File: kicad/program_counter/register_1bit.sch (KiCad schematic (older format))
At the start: 5 parts, among them U1 SN74ALVC00, U2 SN74ALVC00, U3 SN74ALVC00, U4 SN74ALVC00, U5 SN74ALVC00

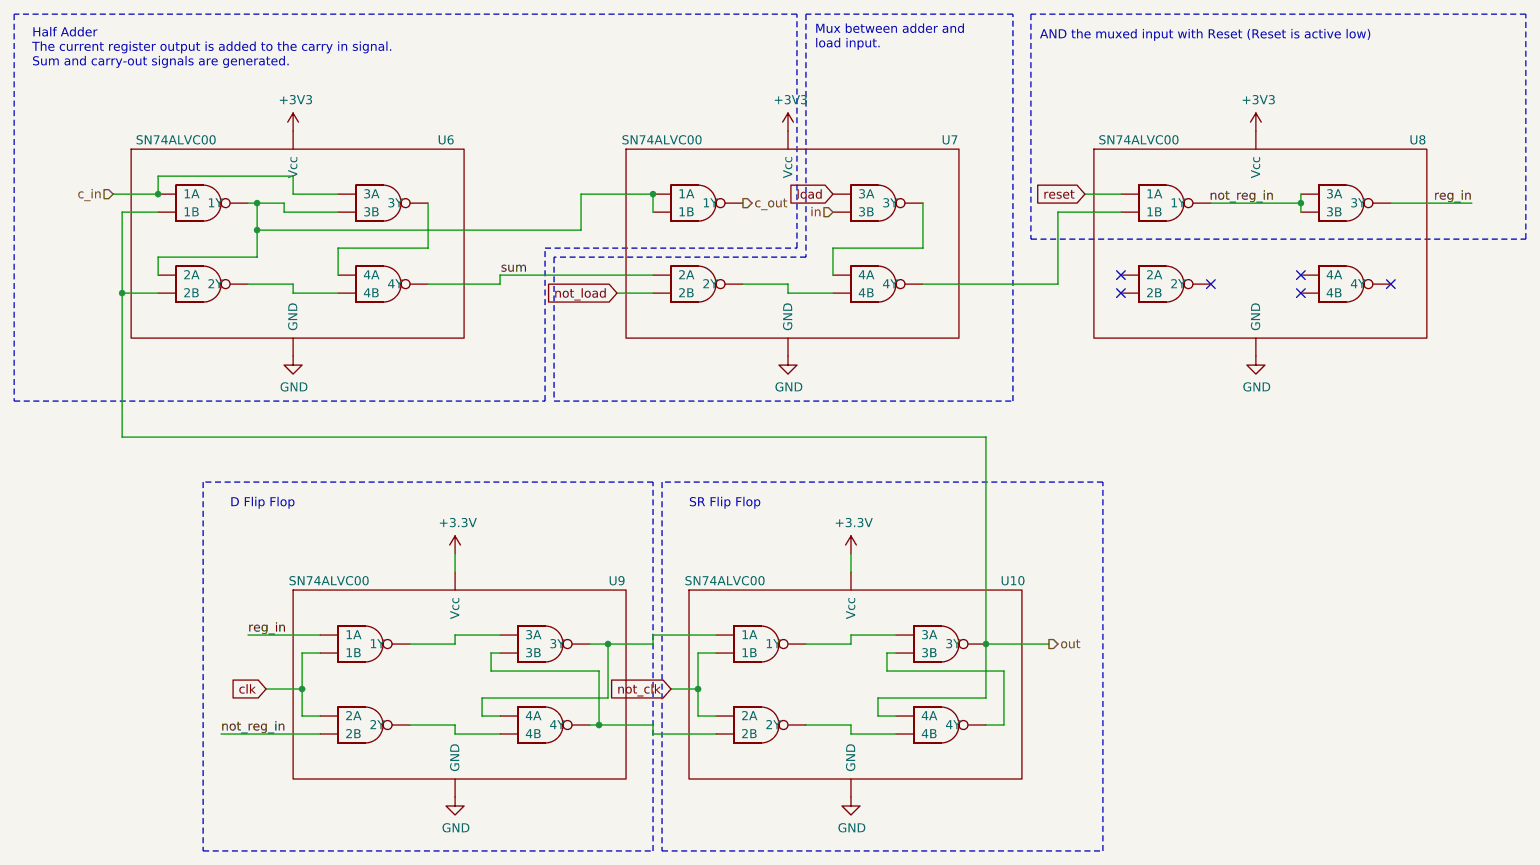
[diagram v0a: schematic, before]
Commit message: ALU schematic, layout, routing complete. Associated motherboardmod. Also added Load LED to register and program counter boards.
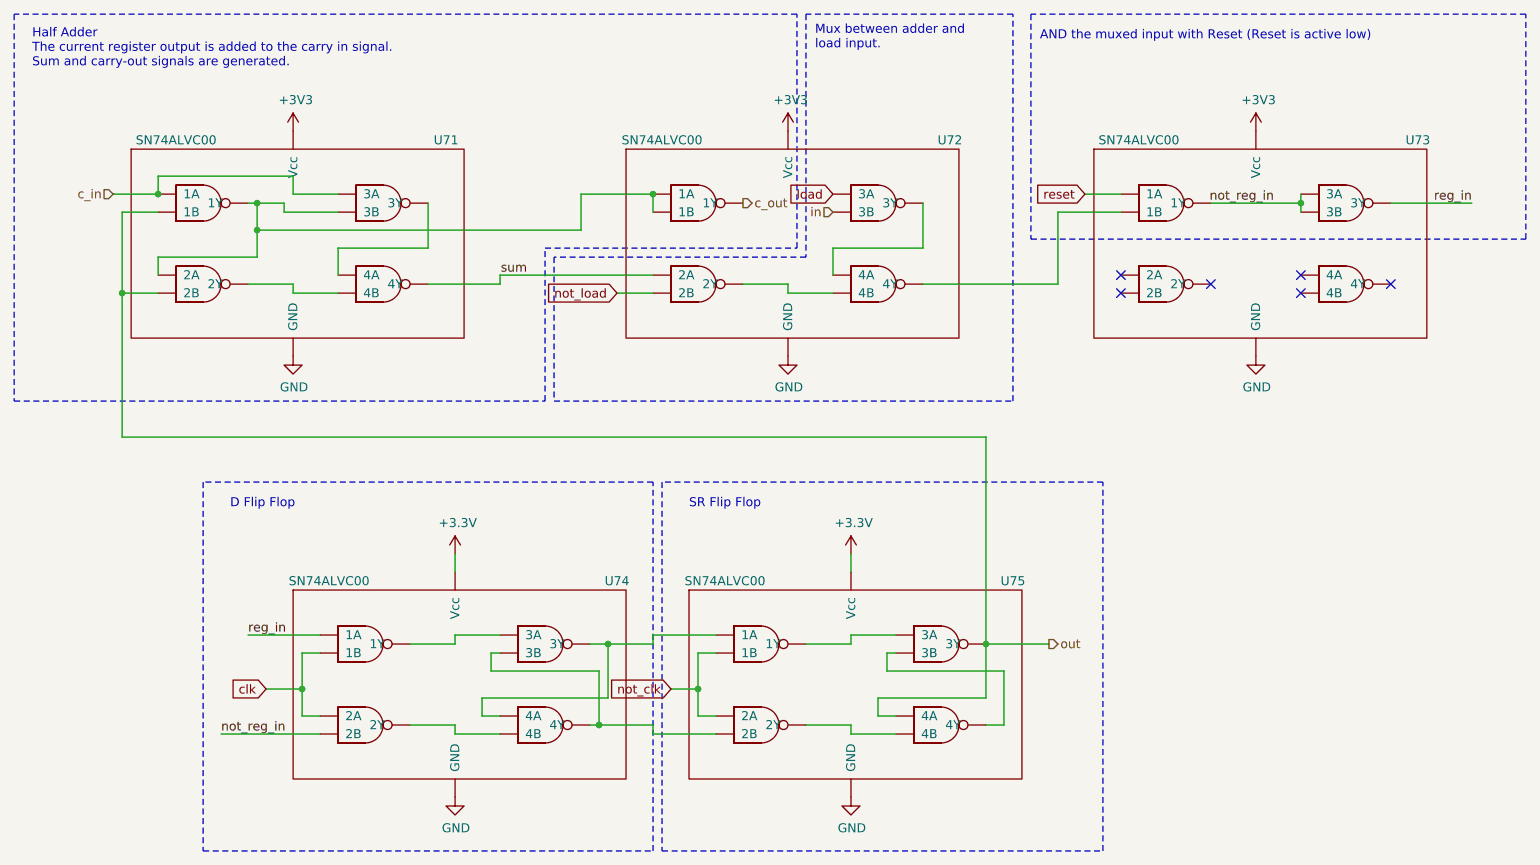
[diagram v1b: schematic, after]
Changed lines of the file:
@@
 $Descr A4 11693 8268
 encoding utf-8
-Sheet 2 16
+Sheet 11 16
 Title "1-bit Register"
 Date "2020-03-15"
@@
 AR Path="/5EC1DD9B/5E702849" Ref="U15"  Part="1"
 AR Path="/5EC1DDBF/5E702849" Ref="U10"  Part="1"
-F 0 "U10" H 7450 3800 50  0000 C CNN
+F 0 "U75" H 7450 3800 50  0000 C CNN
 F 1 "SN74ALVC00" H 5850 3800 50  0000 C CNN
 F 2 "Package_SO:TSSOP-14_4.4x5mm_P0.65mm" H 6550 2650 50  0001 C CNN
@@
 AR Path="/5EC1DD9B/5E6F4B7A" Ref="U14"  Part="1"
 AR Path="/5EC1DDBF/5E6F4B7A" Ref="U9"  Part="1"
-F 0 "U9" H 5250 3800 50  0000 C CNN
+F 0 "U74" H 5250 3800 50  0000 C CNN
 F 1 "SN74ALVC00" H 3650 3800 50  0000 C CNN
 F 2 "Package_SO:TSSOP-14_4.4x5mm_P0.65mm" H 4350 2650 50  0001 C CNN
@@
 AR Path="/5EC1DD9B/5EA8676E" Ref="U13"  Part="1"
 AR Path="/5EC1DDBF/5EA8676E" Ref="U8"  Part="1"
-F 0 "U8" H 9700 1350 50  0000 C CNN
+F 0 "U73" H 9700 1350 50  0000 C CNN
 F 1 "SN74ALVC00" H 8150 1350 50  0000 C CNN
 F 2 "Package_SO:TSSOP-14_4.4x5mm_P0.65mm" H 8800 200 50  0001 C CNN
@@
 AR Path="/5EC1DD9B/5EA8671D" Ref="U12"  Part="1"
 AR Path="/5EC1DDBF/5EA8671D" Ref="U7"  Part="1"
-F 0 "U7" H 7100 1350 50  0000 C CNN
+F 0 "U72" H 7100 1350 50  0000 C CNN
 F 1 "SN74ALVC00" H 5500 1350 50  0000 C CNN
 F 2 "Package_SO:TSSOP-14_4.4x5mm_P0.65mm" H 6200 200 50  0001 C CNN
@@
 AR Path="/5EC1DD9B/5EA86726" Ref="U11"  Part="1"
 AR Path="/5EC1DDBF/5EA86726" Ref="U6"  Part="1"
-F 0 "U6" H 4300 1350 50  0000 C CNN
+F 0 "U71" H 4300 1350 50  0000 C CNN
 F 1 "SN74ALVC00" H 2800 1350 50  0000 C CNN
 F 2 "Package_SO:TSSOP-14_4.4x5mm_P0.65mm" H 3450 200 50  0001 C CNN

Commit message: Readme updates (#6)
* Readme intro section

* Board revisions for manufacturing, add digikey PNs to all, added logo.
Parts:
- U1, U2, U3, U4, U5: Digikey PN (none) -> 296-5104-1-ND
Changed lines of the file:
@@
 $Descr A4 11693 8268
 encoding utf-8
-Sheet 11 16
+Sheet 13 16
 Title "1-bit Register"
 Date "2020-03-15"
@@
 F 2 "Package_SO:TSSOP-14_4.4x5mm_P0.65mm" H 6550 2650 50  0001 C CNN
 F 3 "" H 6800 4150 50  0001 C CNN
+F 4 "296-5104-1-ND" H 0   0   50  0001 C CNN "Digikey PN"
 	1    6800 4150
 	1    0    0    -1
@@
 F 2 "Package_SO:TSSOP-14_4.4x5mm_P0.65mm" H 4350 2650 50  0001 C CNN
 F 3 "" H 4600 4150 50  0001 C CNN
+F 4 "296-5104-1-ND" H 0   0   50  0001 C CNN "Digikey PN"
 	1    4600 4150
 	1    0    0    -1
@@
 F 2 "Package_SO:TSSOP-14_4.4x5mm_P0.65mm" H 8800 200 50  0001 C CNN
 F 3 "" H 9050 1700 50  0001 C CNN
+F 4 "296-5104-1-ND" H 0   0   50  0001 C CNN "Digikey PN"
 	1    9050 1700
 	1    0    0    -1
@@
 F 2 "Package_SO:TSSOP-14_4.4x5mm_P0.65mm" H 6200 200 50  0001 C CNN
 F 3 "" H 6450 1700 50  0001 C CNN
+F 4 "296-5104-1-ND" H 0   0   50  0001 C CNN "Digikey PN"
 	1    6450 1700
 	1    0    0    -1
@@
 F 2 "Package_SO:TSSOP-14_4.4x5mm_P0.65mm" H 3450 200 50  0001 C CNN
 F 3 "" H 3700 1700 50  0001 C CNN
+F 4 "296-5104-1-ND" H 0   0   50  0001 C CNN "Digikey PN"
 	1    3700 1700
 	1    0    0    -1
